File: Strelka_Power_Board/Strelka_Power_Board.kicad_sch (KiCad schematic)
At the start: 22 parts

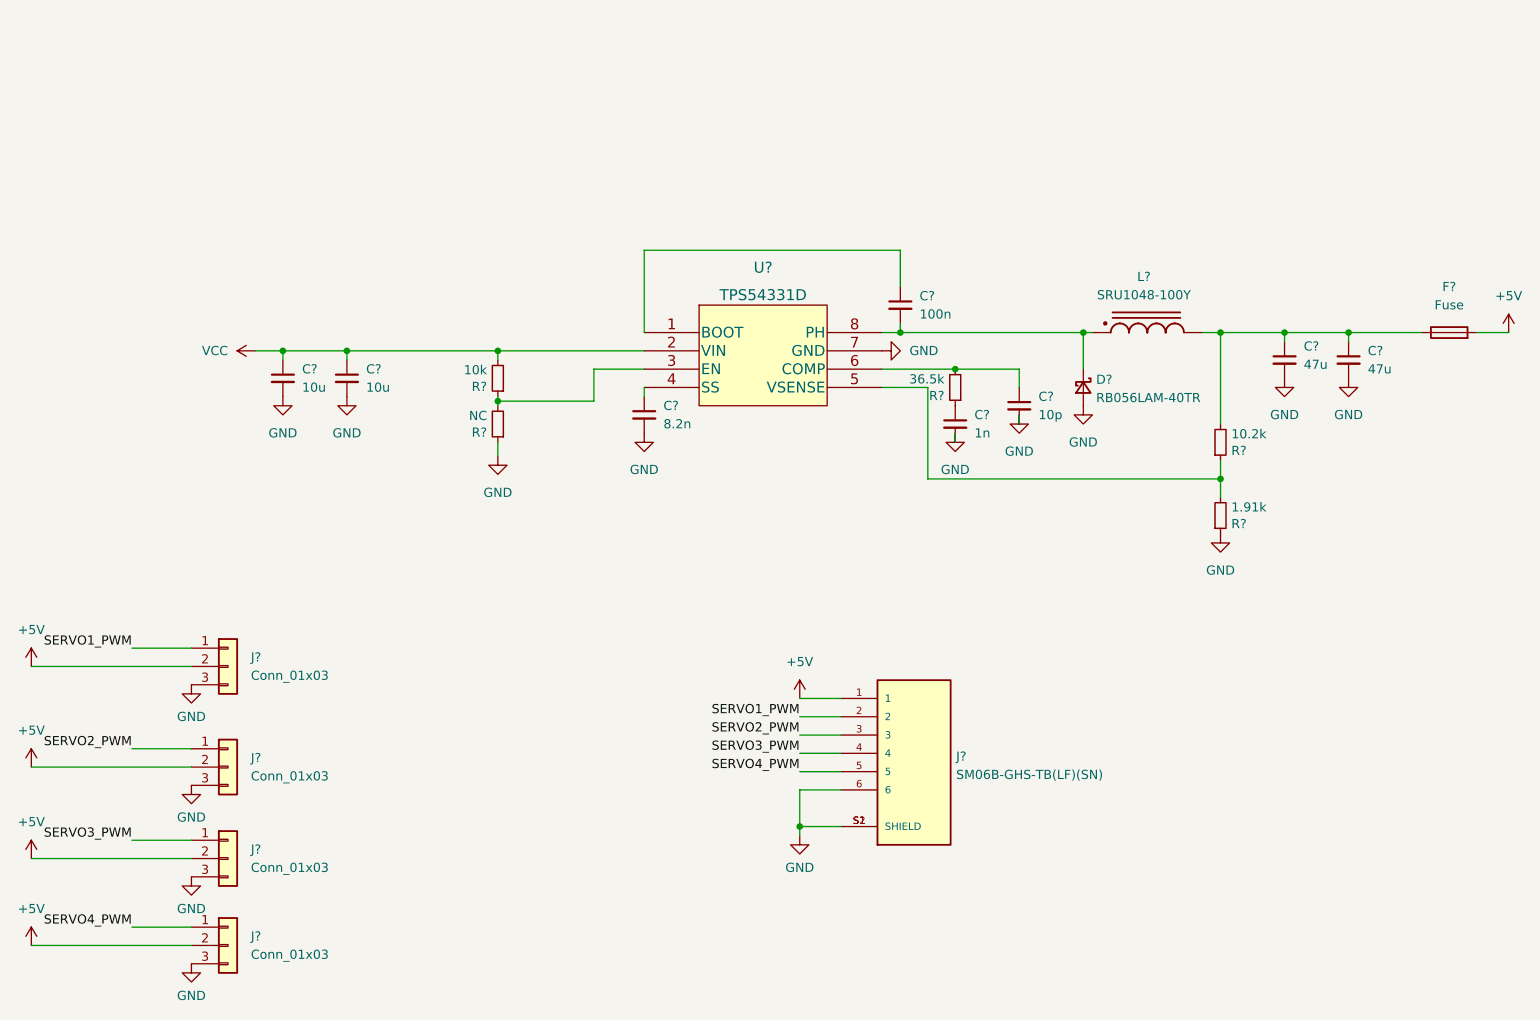
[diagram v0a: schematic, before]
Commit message: Added motor driver to power board
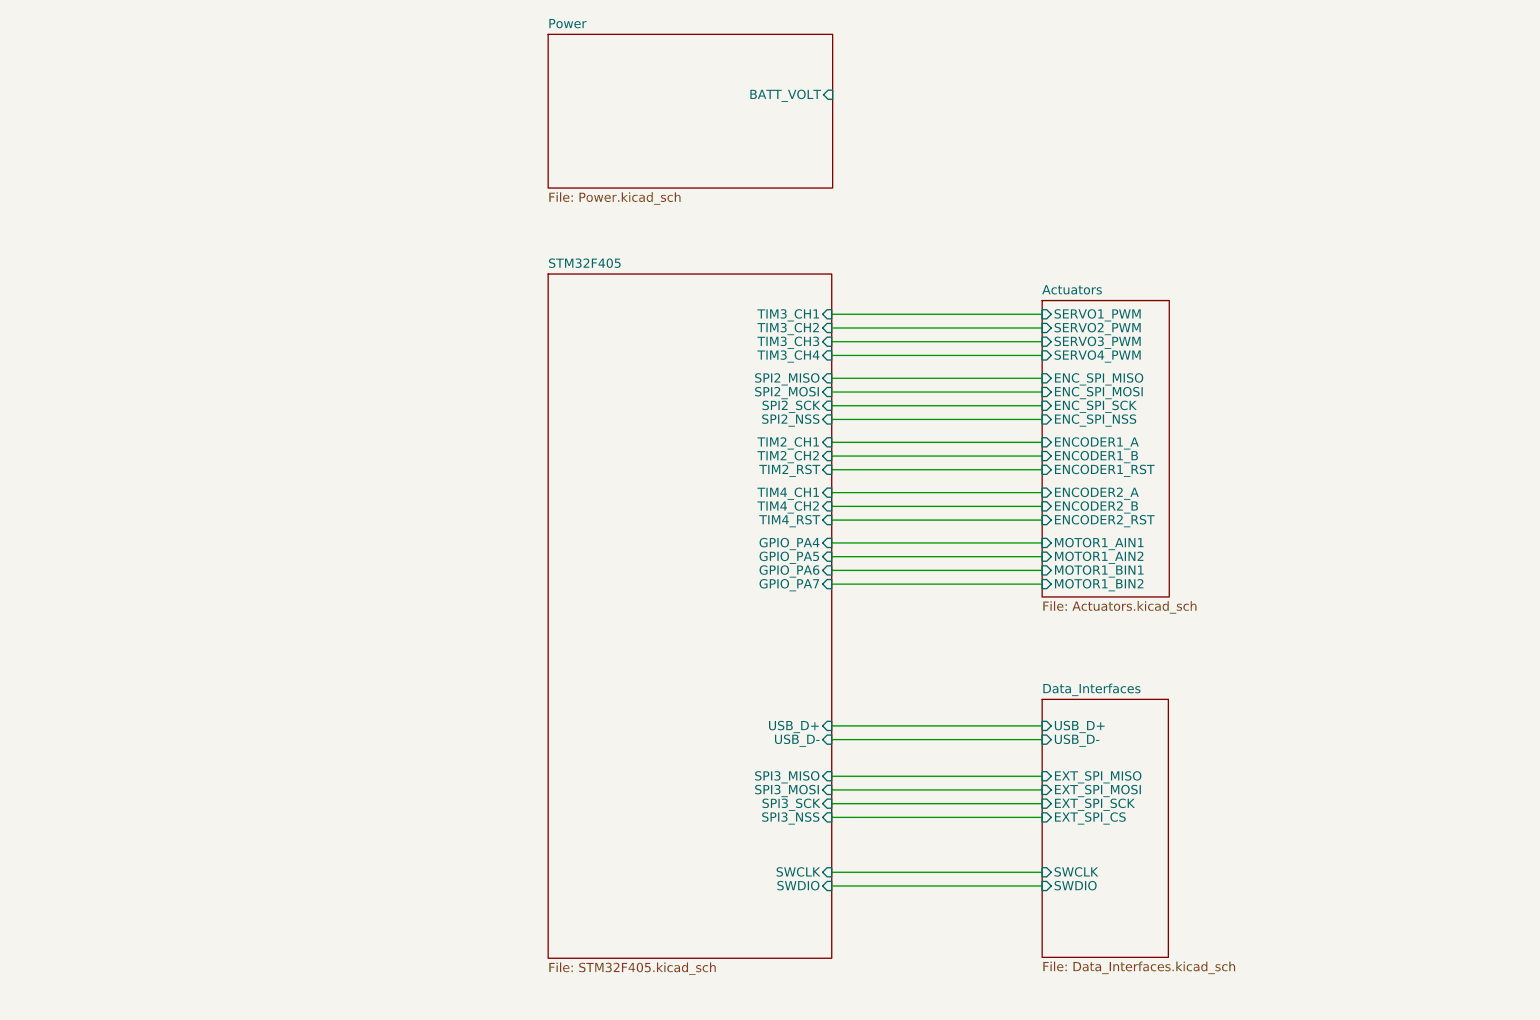
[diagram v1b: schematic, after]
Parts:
- removed C?: 1n, Capacitor_SMD:C_0805_2012Metric_Pad1.18x1.45mm_HandSolder, symbol Device:C_Small
- removed C? (x2): 47u, Capacitor_SMD:C_0805_2012Metric_Pad1.18x1.45mm_HandSolder, symbol Device:C_Small
- removed C? (x2): 10u, Capacitor_SMD:C_0805_2012Metric_Pad1.18x1.45mm_HandSolder, symbol Device:C_Small
- removed C?: 100n, Capacitor_SMD:C_0805_2012Metric_Pad1.18x1.45mm_HandSolder, symbol Device:C_Small
- removed C?: 10p, Capacitor_SMD:C_0805_2012Metric_Pad1.18x1.45mm_HandSolder, symbol Device:C_Small
- removed C?: 8.2n, Capacitor_SMD:C_0805_2012Metric_Pad1.18x1.45mm_HandSolder, symbol Device:C_Small
- removed D?: RB056LAM-40TR, Footprints:RB056LAM-40TR, symbol Device:D_Schottky_Small
- removed F?: Fuse, Resistor_SMD:R_0603_1608Metric, symbol Device:Fuse
- removed J? (x4): Conn_01x03, symbol Connector_Generic:Conn_01x03
- removed J?: SM06B-GHS-TB(LF)(SN), Footprints:JST_SM06B-GHS-TB(LF)(SN), symbol SM06B-GHS-TB_LF__SN_:SM06B-GHS-TB(LF)(SN)
- removed L?: SRU1048-100Y, Footprints:IND_SRU1048-100Y, symbol SRU1048-100Y:SRU1048-100Y
- removed R?: NC, Resistor_SMD:R_0603_1608Metric, symbol Device:R_Small
- removed R?: 36.5k, Resistor_SMD:R_0603_1608Metric, symbol Device:R_Small
- removed R?: 10.2k, Resistor_SMD:R_0603_1608Metric, symbol Device:R_Small
- removed R?: 1.91k, Resistor_SMD:R_0603_1608Metric, symbol Device:R_Small
- removed R?: 10k, Resistor_SMD:R_0603_1608Metric, symbol Device:R_Small
- removed U?: TPS54331D, Footprints:TPS54331D, symbol TPS54331D:TPS54331D
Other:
- added sheet Actuators (Actuators.kicad_sch)
- added sheet Data_Interfaces (Data_Interfaces.kicad_sch)
- added sheet Power (Power.kicad_sch)
- added sheet STM32F405 (STM32F405.kicad_sch)
